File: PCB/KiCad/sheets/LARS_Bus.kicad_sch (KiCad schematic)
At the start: 24 parts, among them J28 USB1, J29 USB2, U10 USBLC6-2SC6, U11 TCAN1057AVDRQ1, U12 USBLC6-2SC6

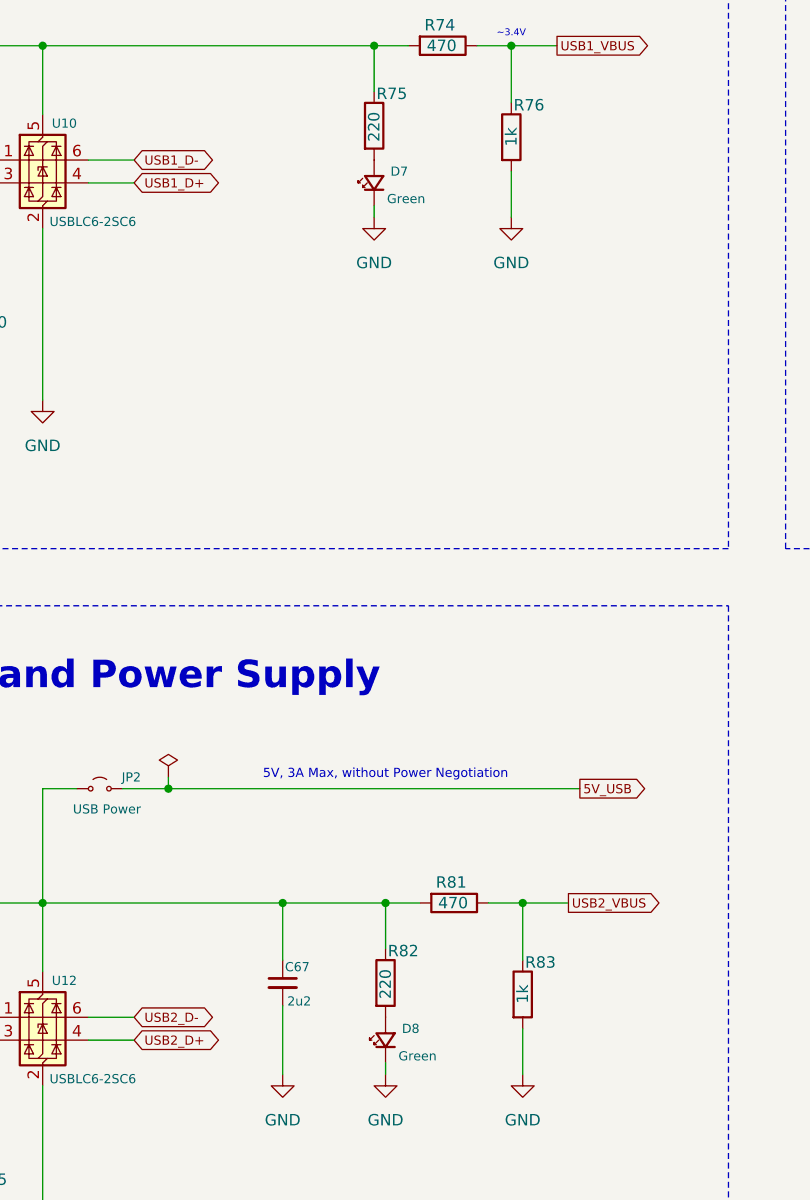
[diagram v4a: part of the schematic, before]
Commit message: add ESD protection and update footprints
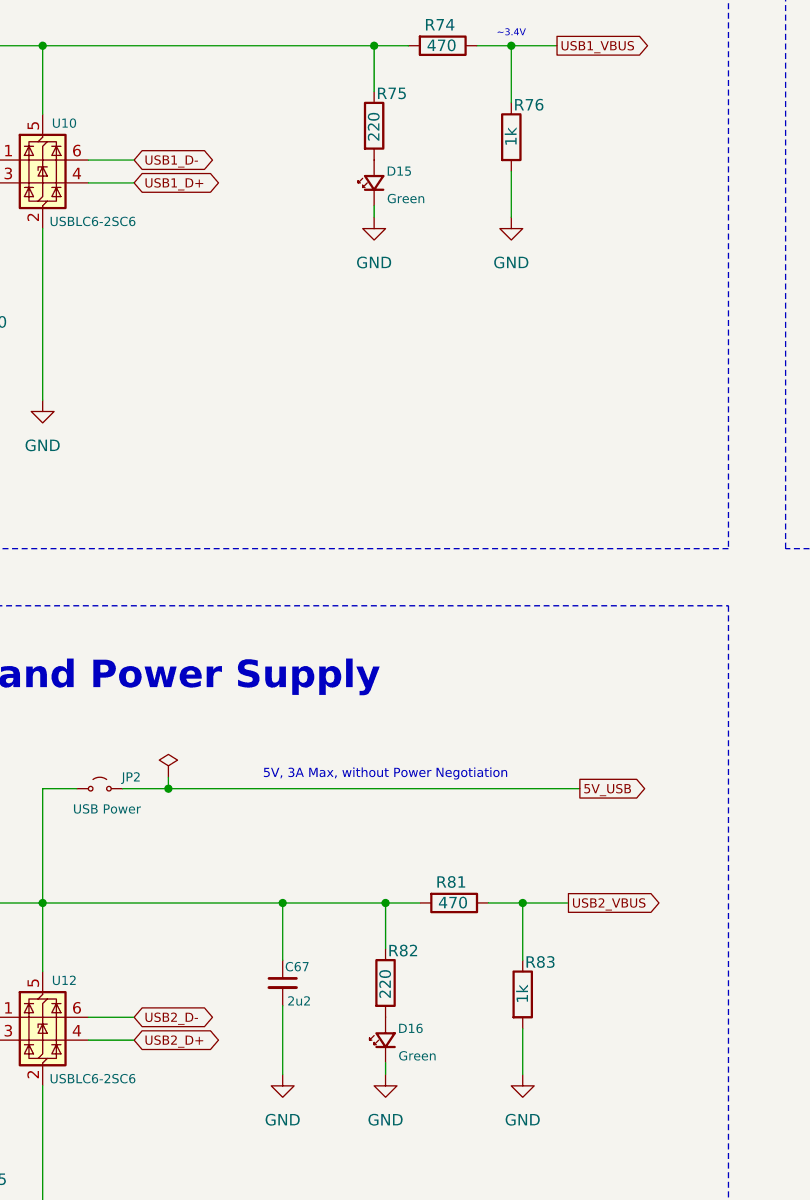
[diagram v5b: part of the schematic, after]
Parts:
- renumbered D7 to D15, D8 to D16
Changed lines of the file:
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@@
 		(dnp no)
 		(fields_autoplaced yes)
-		(property "Reference" "#PWR0168"
+		(property "Reference" "#PWR0175"
 			(at 123.19 67.31 0)
 			(effects
@@
 			(project "hardware_interface"
 				(path "/ffedf44c-a51a-4124-b6d3-e3f1f256e9ac/31b4cc6e-8490-43f3-a459-a8f45a93fb3e"
-					(reference "#PWR0168")
+					(reference "#PWR0175")
 					(unit 1)
 				)
@@
 		(dnp no)
 		(fields_autoplaced yes)
-		(property "Reference" "#PWR0170"
+		(property "Reference" "#PWR0177"
 			(at 170.18 78.74 0)
 			(effects
@@
 			(project "hardware_interface"
 				(path "/ffedf44c-a51a-4124-b6d3-e3f1f256e9ac/31b4cc6e-8490-43f3-a459-a8f45a93fb3e"
-					(reference "#PWR0170")
+					(reference "#PWR0177")
 					(unit 1)
 				)
@@
 		(dnp no)
 		(fields_autoplaced yes)
-		(property "Reference" "#PWR0175"
+		(property "Reference" "#PWR0182"
 			(at 63.5 87.63 0)
 			(effects
@@
 			(project "hardware_interface"
 				(path "/ffedf44c-a51a-4124-b6d3-e3f1f256e9ac/31b4cc6e-8490-43f3-a459-a8f45a93fb3e"
-					(reference "#PWR0175")
+					(reference "#PWR0182")
 					(unit 1)
 				)
@@
 		(dnp no)
 		(fields_autoplaced yes)
-		(property "Reference" "#PWR0165"
+		(property "Reference" "#PWR0172"
 			(at 163.83 44.45 0)
 			(effects
@@
 			(project "hardware_interface"
 				(path "/ffedf44c-a51a-4124-b6d3-e3f1f256e9ac/31b4cc6e-8490-43f3-a459-a8f45a93fb3e"
-					(reference "#PWR0165")
+					(reference "#PWR0172")
 					(unit 1)
 				)
@@
 		(dnp no)
 		(fields_autoplaced yes)
-		(property "Reference" "#PWR0169"
+		(property "Reference" "#PWR0176"
 			(at 163.83 78.74 0)
 			(effects
@@
 			(project "hardware_interface"
 				(path "/ffedf44c-a51a-4124-b6d3-e3f1f256e9ac/31b4cc6e-8490-43f3-a459-a8f45a93fb3e"
-					(reference "#PWR0169")
+					(reference "#PWR0176")
 					(unit 1)
 				)
@@
 		(dnp no)
 		(fields_autoplaced yes)
-		(property "Reference" "#PWR0178"
+		(property "Reference" "#PWR0185"
 			(at 109.22 162.56 0)
 			(effects
@@
 			(project "hardware_interface"
 				(path "/ffedf44c-a51a-4124-b6d3-e3f1f256e9ac/31b4cc6e-8490-43f3-a459-a8f45a93fb3e"
-					(reference "#PWR0178")
+					(reference "#PWR0185")
 					(unit 1)
 				)
@@
 		(dnp no)
 		(fields_autoplaced yes)
-		(property "Reference" "#PWR0182"
+		(property "Reference" "#PWR0189"
 			(at 55.88 182.88 0)
 			(effects
@@
 			(project "hardware_interface"
 				(path "/ffedf44c-a51a-4124-b6d3-e3f1f256e9ac/31b4cc6e-8490-43f3-a459-a8f45a93fb3e"
-					(reference "#PWR0182")
+					(reference "#PWR0189")
 					(unit 1)
 				)
@@
 		(dnp no)
 		(fields_autoplaced yes)
-		(property "Reference" "#PWR0171"
+		(property "Reference" "#PWR0178"
 			(at 190.5 78.74 0)
 			(effects
@@
 			(project "hardware_interface"
 				(path "/ffedf44c-a51a-4124-b6d3-e3f1f256e9ac/31b4cc6e-8490-43f3-a459-a8f45a93fb3e"
-					(reference "#PWR0171")
+					(reference "#PWR0178")
 					(unit 1)
 				)
@@
 		(dnp no)
 		(fields_autoplaced yes)
-		(property "Reference" "#PWR0179"
+		(property "Reference" "#PWR0186"
 			(at 124.46 162.56 0)
 			(effects
@@
 			(project "hardware_interface"
 				(path "/ffedf44c-a51a-4124-b6d3-e3f1f256e9ac/31b4cc6e-8490-43f3-a459-a8f45a93fb3e"
-					(reference "#PWR0179")
+					(reference "#PWR0186")
 					(unit 1)
 				)
@@
 		(dnp no)
 		(fields_autoplaced yes)
-		(property "Reference" "#PWR0172"
+		(property "Reference" "#PWR0179"
 			(at 29.21 87.63 0)
 			(effects
@@
 			(project "hardware_interface"
 				(path "/ffedf44c-a51a-4124-b6d3-e3f1f256e9ac/31b4cc6e-8490-43f3-a459-a8f45a93fb3e"
-					(reference "#PWR0172")
+					(reference "#PWR0179")
 					(unit 1)
 				)
@@
 		(on_board yes)
 		(dnp no)
-		(property "Reference" "D7"
+		(property "Reference" "D15"
 			(at 110.744 55.88 90)
 			(effects
@@
 			(project "hardware_interface"
 				(path "/ffedf44c-a51a-4124-b6d3-e3f1f256e9ac/31b4cc6e-8490-43f3-a459-a8f45a93fb3e"
-					(reference "D7")
+					(reference "D15")
 					(unit 1)
 				)
@@
 		(dnp no)
 		(fields_autoplaced yes)
-		(property "Reference" "#PWR0184"
+		(property "Reference" "#PWR0191"
 			(at 71.12 182.88 0)
 			(effects
@@
 			(project "hardware_interface"
 				(path "/ffedf44c-a51a-4124-b6d3-e3f1f256e9ac/31b4cc6e-8490-43f3-a459-a8f45a93fb3e"
-					(reference "#PWR0184")
+					(reference "#PWR0191")
 					(unit 1)
 				)
@@
 		(dnp no)
 		(fields_autoplaced yes)
-		(property "Reference" "#PWR0173"
+		(property "Reference" "#PWR0180"
 			(at 36.83 87.63 0)
 			(effects
@@
 			(project "hardware_interface"
 				(path "/ffedf44c-a51a-4124-b6d3-e3f1f256e9ac/31b4cc6e-8490-43f3-a459-a8f45a93fb3e"
-					(reference "#PWR0173")
+					(reference "#PWR0180")
 					(unit 1)
 				)
@@
 		(dnp no)
 		(fields_autoplaced yes)
-		(property "Reference" "#PWR0176"
+		(property "Reference" "#PWR0183"
 			(at 71.12 87.63 0)
 			(effects
@@
 			(project "hardware_interface"
 				(path "/ffedf44c-a51a-4124-b6d3-e3f1f256e9ac/31b4cc6e-8490-43f3-a459-a8f45a93fb3e"
-					(reference "#PWR0176")
+					(reference "#PWR0183")
 					(unit 1)
 				)
@@
 		(dnp no)
 		(fields_autoplaced yes)
-		(property "Reference" "#PWR0174"
+		(property "Reference" "#PWR0181"
 			(at 55.88 87.63 0)
 			(effects
@@
 			(project "hardware_interface"
 				(path "/ffedf44c-a51a-4124-b6d3-e3f1f256e9ac/31b4cc6e-8490-43f3-a459-a8f45a93fb3e"
-					(reference "#PWR0174")
+					(reference "#PWR0181")
 					(unit 1)
 				)
@@
 		(dnp no)
 		(fields_autoplaced yes)
-		(property "Reference" "#PWR0167"
+		(property "Reference" "#PWR0174"
 			(at 107.95 67.31 0)
 			(effects
@@
 			(project "hardware_interface"
 				(path "/ffedf44c-a51a-4124-b6d3-e3f1f256e9ac/31b4cc6e-8490-43f3-a459-a8f45a93fb3e"
-					(reference "#PWR0167")
+					(reference "#PWR0174")
 					(unit 1)
 				)
@@
 		(dnp no)
 		(fields_autoplaced yes)
-		(property "Reference" "#PWR0166"
+		(property "Reference" "#PWR0173"
 			(at 170.18 44.45 0)
 			(effects
@@
 			(project "hardware_interface"
 				(path "/ffedf44c-a51a-4124-b6d3-e3f1f256e9ac/31b4cc6e-8490-43f3-a459-a8f45a93fb3e"
-					(reference "#PWR0166")
+					(reference "#PWR0173")
 					(unit 1)
 				)
@@
 		(dnp no)
 		(fields_autoplaced yes)
-		(property "Reference" "#PWR0181"
+		(property "Reference" "#PWR0188"
 			(at 36.83 182.88 0)
 			(effects
@@
 			(project "hardware_interface"
 				(path "/ffedf44c-a51a-4124-b6d3-e3f1f256e9ac/31b4cc6e-8490-43f3-a459-a8f45a93fb3e"
-					(reference "#PWR0181")
+					(reference "#PWR0188")
 					(unit 1)
 				)
@@
 		(on_board yes)
 		(dnp no)
-		(property "Reference" "D8"
+		(property "Reference" "D16"
 			(at 112.014 151.13 90)
 			(effects
@@
 			(project "hardware_interface"
 				(path "/ffedf44c-a51a-4124-b6d3-e3f1f256e9ac/31b4cc6e-8490-43f3-a459-a8f45a93fb3e"
-					(reference "D8")
+					(reference "D16")
 					(unit 1)
 				)
@@
 		(dnp no)
 		(fields_autoplaced yes)
-		(property "Reference" "#PWR0183"
+		(property "Reference" "#PWR0190"
 			(at 63.5 182.88 0)
 			(effects
@@
 			(project "hardware_interface"
 				(path "/ffedf44c-a51a-4124-b6d3-e3f1f256e9ac/31b4cc6e-8490-43f3-a459-a8f45a93fb3e"
-					(reference "#PWR0183")
+					(reference "#PWR0190")
 					(unit 1)
 				)
@@
 		(dnp no)
 		(fields_autoplaced yes)
-		(property "Reference" "#PWR0177"
+		(property "Reference" "#PWR0184"
 			(at 97.79 162.56 0)
 			(effects
@@
 			(project "hardware_interface"
 				(path "/ffedf44c-a51a-4124-b6d3-e3f1f256e9ac/31b4cc6e-8490-43f3-a459-a8f45a93fb3e"
-					(reference "#PWR0177")
+					(reference "#PWR0184")
 					(unit 1)
 				)
@@
 		(dnp no)
 		(fields_autoplaced yes)
-		(property "Reference" "#PWR0180"
+		(property "Reference" "#PWR0187"
 			(at 29.21 182.88 0)
 			(effects
@@
 			(project "hardware_interface"
 				(path "/ffedf44c-a51a-4124-b6d3-e3f1f256e9ac/31b4cc6e-8490-43f3-a459-a8f45a93fb3e"
-					(reference "#PWR0180")
-					(unit 1)
-				)
+					(reference "#PWR0187")
+					(unit 1)
+				)

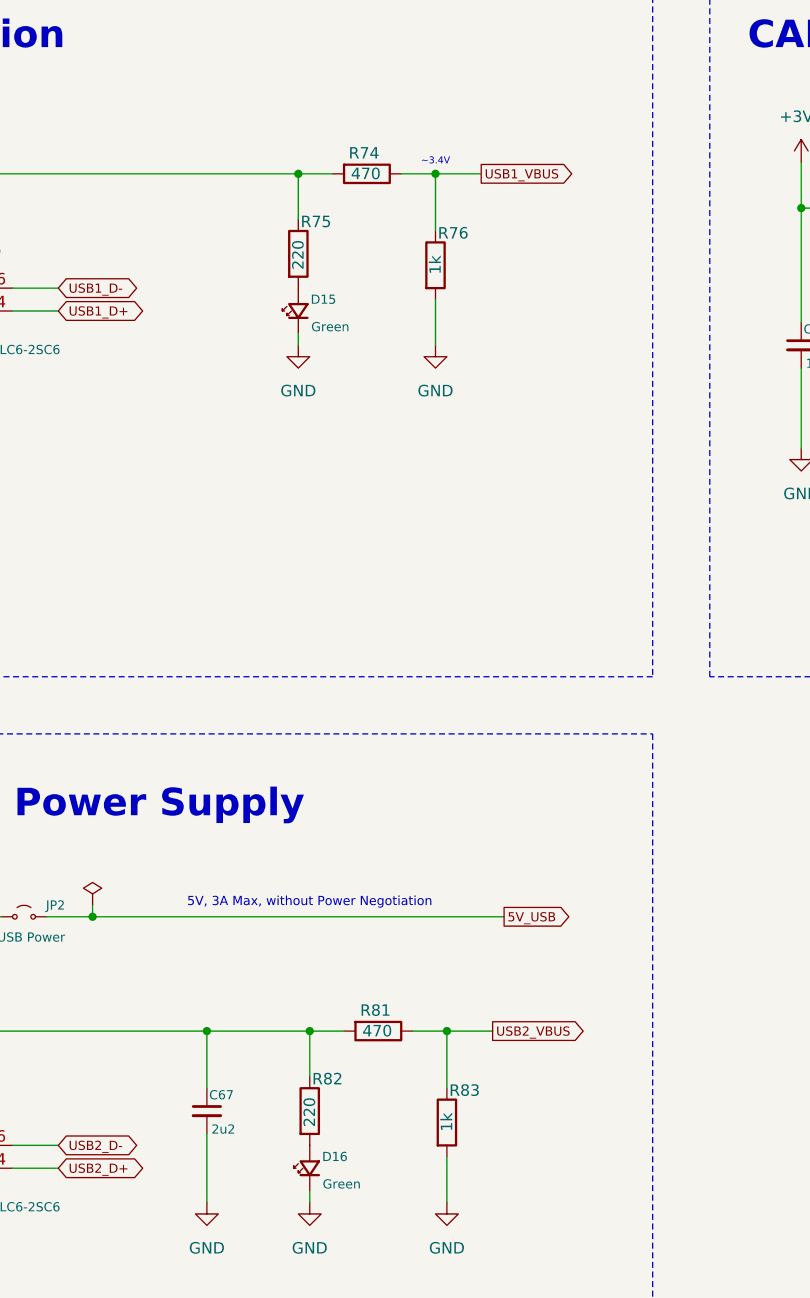
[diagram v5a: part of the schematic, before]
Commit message: PCB: update resistor values and embed font
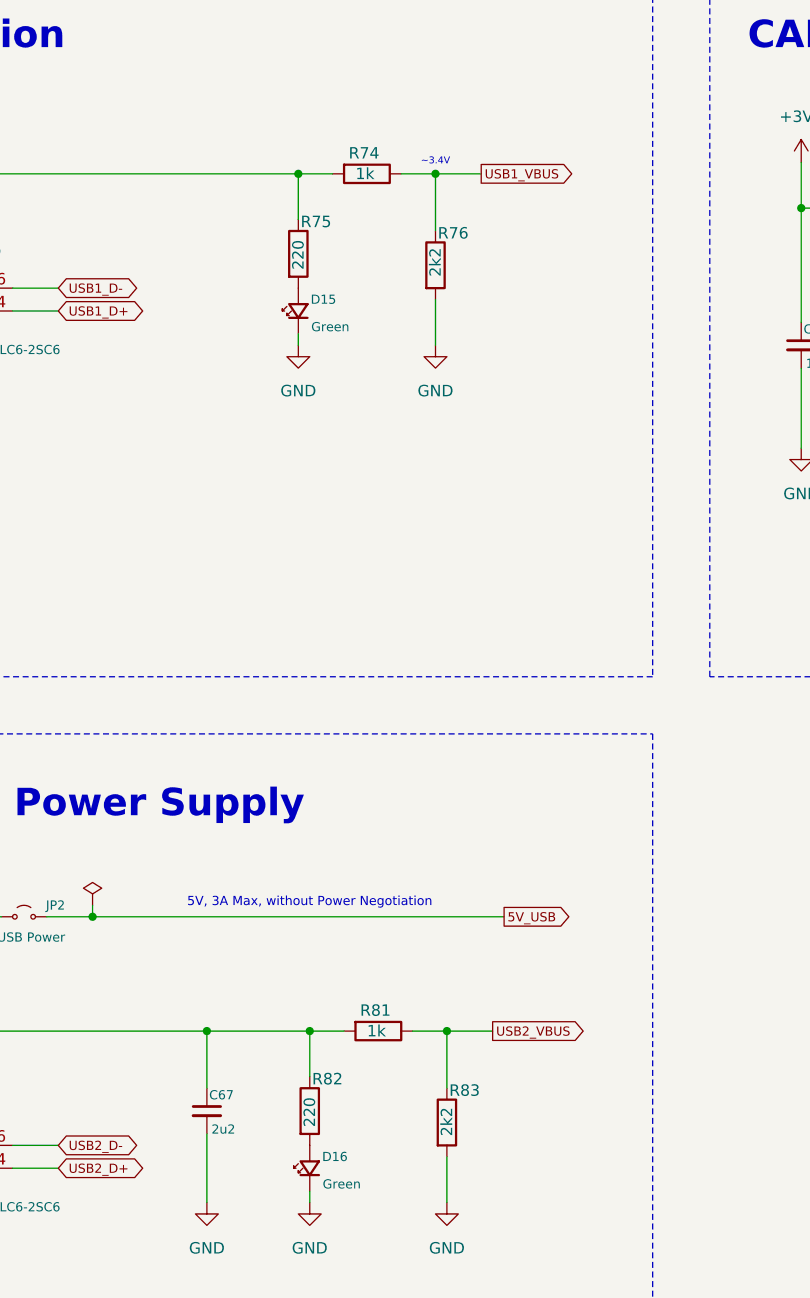
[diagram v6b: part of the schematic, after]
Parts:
- R74, R81: value 470 -> 1k
- R76, R83: value 1k -> 2k2
